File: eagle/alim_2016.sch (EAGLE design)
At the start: 54 parts, among them J1 AVR_SPI_PRG_6PTH, J2 AVR_SPI_PRG_6PTH, U1 3.3V, U2 LM2678S-5.0, U4 LM2596S-ADJ, U5 ATTINY85-20SU, U6 ATMEGA328P_TQFP

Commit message: clean up board
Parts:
- added C5: 10n, rcl:C-EUC0805
- added U$29: SRR1260, alim:SRR1260
- added U$30: SBRS8340, alim:SBRS8340
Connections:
- net N$12 renamed 24V
- new net N$29: C5.2, U$29.1, U$30.P$2, U2.SW
- new net N$30: C5.1, U2.BOOST
- net 5.0V: now also U$29.2, U2.FB
- net GND: now also U$30.P$1
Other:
- moved on the sheet: U2
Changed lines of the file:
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@@
 <layer number="230" name="230bmp" color="7" fill="1" visible="yes" active="yes"/>
 <layer number="231" name="231bmp" color="7" fill="1" visible="yes" active="yes"/>
+<layer number="232" name="Eagle3D_PG2" color="7" fill="1" visible="no" active="no"/>
+<layer number="233" name="Eagle3D_PG3" color="7" fill="1" visible="no" active="no"/>
 <layer number="248" name="Housing" color="7" fill="1" visible="yes" active="yes"/>
 <layer number="249" name="Edge" color="7" fill="1" visible="yes" active="yes"/>
@@
 <part name="R19" library="resistor" deviceset="R-EU_" device="M0805" value="220"/>
 <part name="U$28" library="microbuilder" deviceset="GND" device=""/>
+<part name="U$29" library="alim" deviceset="SRR1260" device=""/>
+<part name="C5" library="rcl" deviceset="C-EU" device="C0805" value="10n"/>
+<part name="U$30" library="alim" deviceset="SBRS8340" device=""/>
+<part name="U$31" library="microbuilder" deviceset="GND" device=""/>
+<part name="U$32" library="microbuilder" deviceset="5.0V" device=""/>
 </parts>
 <sheets>
@@
 <instance part="U$7" gate="G$1" x="124.46" y="-12.7"/>
 <instance part="U2" gate="A" x="106.68" y="55.88"/>
-<instance part="U$22" gate="G$1" x="88.9" y="45.72"/>
+<instance part="U$22" gate="G$1" x="106.68" y="43.18"/>
 <instance part="U4" gate="A" x="104.14" y="22.86"/>
 <instance part="U$23" gate="G$1" x="88.9" y="10.16"/>
@@
 <instance part="R5" gate="G$1" x="-27.94" y="30.48" rot="R180"/>
 <instance part="S1" gate="G$1" x="-22.86" y="38.1" rot="MR90"/>
-<instance part="U$4" gate="G$1" x="88.9" y="58.42"/>
+<instance part="U$4" gate="G$1" x="88.9" y="55.88"/>
 <instance part="12V" gate="-1" x="-2.54" y="43.18"/>
 <instance part="12V" gate="-2" x="-2.54" y="22.86"/>
@@
 <instance part="R19" gate="G$1" x="142.24" y="-91.44" rot="R180"/>
 <instance part="U$28" gate="G$1" x="147.32" y="-99.06"/>
+<instance part="U$29" gate="G$1" x="124.46" y="50.8"/>
+<instance part="C5" gate="G$1" x="114.3" y="55.88" rot="R90"/>
+<instance part="U$30" gate="G$1" x="119.38" y="45.72" rot="R270"/>
+<instance part="U$31" gate="G$1" x="119.38" y="40.64"/>
+<instance part="U$32" gate="G$1" x="134.62" y="53.34"/>
 </instances>
 <busses>
@@
 <pinref part="U$22" gate="G$1" pin="GND"/>
 <pinref part="U2" gate="A" pin="GND_2"/>
-<wire x1="88.9" y1="50.8" x2="88.9" y2="48.26" width="0.1524" layer="91"/>
-<junction x="88.9" y="48.26"/>
+<junction x="106.68" y="45.72"/>
+<wire x1="106.68" y1="45.72" x2="104.14" y2="45.72" width="0.1524" layer="91"/>
 </segment>
 <segment>
@@
 <pinref part="U$28" gate="G$1" pin="GND"/>
 </segment>
+<segment>
+<pinref part="U$30" gate="G$1" pin="P$1"/>
+<pinref part="U$31" gate="G$1" pin="GND"/>
+</segment>
 </net>
 <net name="5.0V" class="0">
@@
 <pinref part="5V" gate="-1" pin="K"/>
 <pinref part="U$3" gate="G$1" pin="5.0V"/>
+</segment>
+<segment>
+<pinref part="U2" gate="A" pin="FB"/>
+<wire x1="101.6" y1="60.96" x2="129.54" y2="60.96" width="0.1524" layer="91"/>
+<pinref part="U$29" gate="G$1" pin="2"/>
+<wire x1="129.54" y1="60.96" x2="129.54" y2="50.8" width="0.1524" layer="91"/>
+<pinref part="U$32" gate="G$1" pin="5.0V"/>
+<wire x1="129.54" y1="50.8" x2="134.62" y2="50.8" width="0.1524" layer="91"/>
+<junction x="129.54" y="50.8"/>
 </segment>
 </net>
@@
 </segment>
 </net>
-<net name="N$12" class="0">
+<net name="24V" class="0">
 <segment>
 <pinref part="BAT2" gate="-1" pin="KL"/>
@@
 <pinref part="U2" gate="A" pin="VIN"/>
 <pinref part="U$4" gate="G$1" pin="12V"/>
+<wire x1="88.9" y1="53.34" x2="91.44" y2="53.34" width="0.1524" layer="91"/>
 </segment>
 </net>
@@
 </segment>
 </net>
+<net name="N$29" class="0">
+<segment>
+<pinref part="U2" gate="A" pin="SW"/>
+<pinref part="U$29" gate="G$1" pin="1"/>
+<pinref part="C5" gate="G$1" pin="2"/>
+<wire x1="119.38" y1="55.88" x2="119.38" y2="50.8" width="0.1524" layer="91"/>
+<junction x="119.38" y="50.8"/>
+<wire x1="119.38" y1="50.8" x2="111.76" y2="50.8" width="0.1524" layer="91"/>
+<pinref part="U$30" gate="G$1" pin="P$2"/>
+</segment>
+</net>
+<net name="N$30" class="0">
+<segment>
+<pinref part="U2" gate="A" pin="BOOST"/>
+<pinref part="C5" gate="G$1" pin="1"/>
+</segment>
+</net>

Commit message: most of the circuit finished
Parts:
- 12V, 24V, 3.3V, 5V, 8V: value 1751248 -> MKDSN1,5/2-5,08; device con-phoenix-350:1751248 -> con-phoenix-508:MKDSN1,5/2-5,08
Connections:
- net 12V: now also 12V-1.KL; no longer 12V-1.K
- net 24V: now also 24V-1.KL; no longer 24V-1.K
- net 5.0V: now also 5V-1.KL; no longer 5V-1.K
- net GND: now also 12V-2.KL, 24V-2.KL, 3.3V-2.KL, 5V-2.KL, 8V-2.KL; no longer 12V-2.K, 24V-2.K, 3.3V-2.K, 5V-2.K, 8V-2.K
- net N$1: now also 3.3V-1.KL; no longer 3.3V-1.K
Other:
- moved on the sheet: BAT1-1, BAT1-2, BAT2-1, BAT2-2, BAT3-1, BAT3-2, C1, C2, C3, C4, C5, D1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

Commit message: more cleanup
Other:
- moved on the sheet: D1, D2, D3, D4, LED1, LED2, LED3, LED4, LED5, LED6, R10, R11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

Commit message: rearrange stuff
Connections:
- net N$29 renamed SW
- net N$30 renamed BOOST
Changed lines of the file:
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@@
 </segment>
 </net>
-<net name="N$29" class="0">
+<net name="SW" class="0">
 <segment>
 <pinref part="U2" gate="A" pin="SW"/>
@@
 </segment>
 </net>
-<net name="N$30" class="0">
+<net name="BOOST" class="0">
 <segment>
 <pinref part="U2" gate="A" pin="BOOST"/>

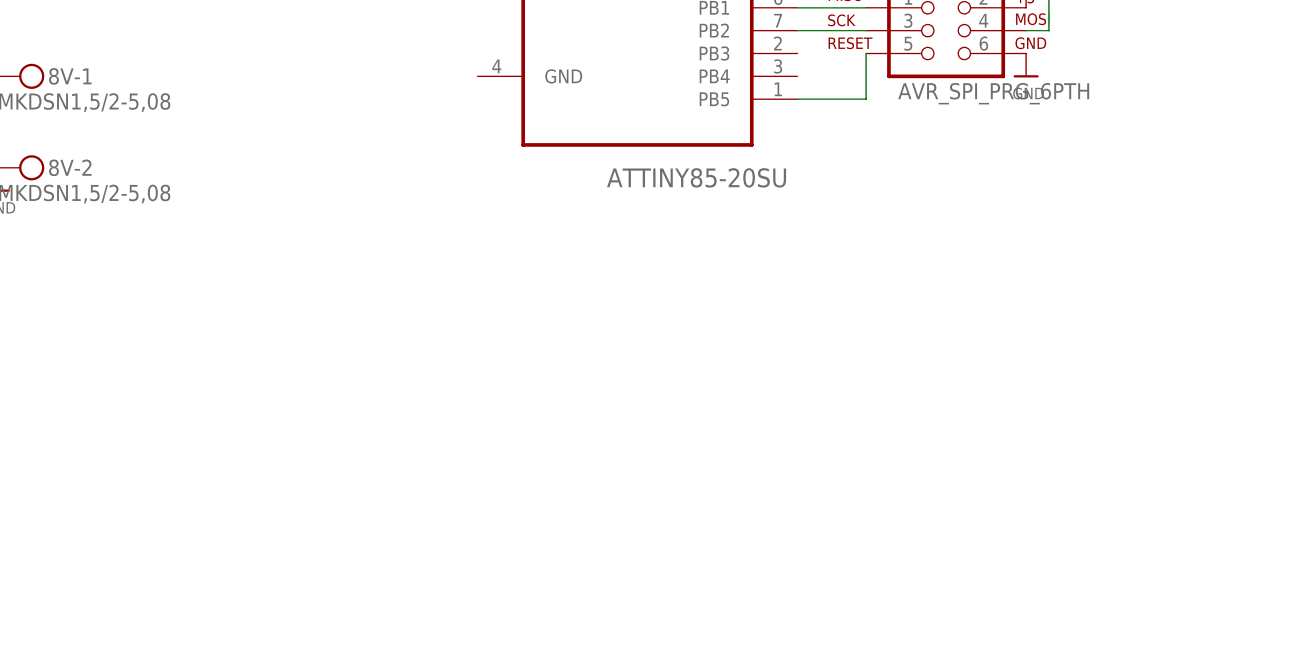
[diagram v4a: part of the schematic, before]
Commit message: add new switching regulator
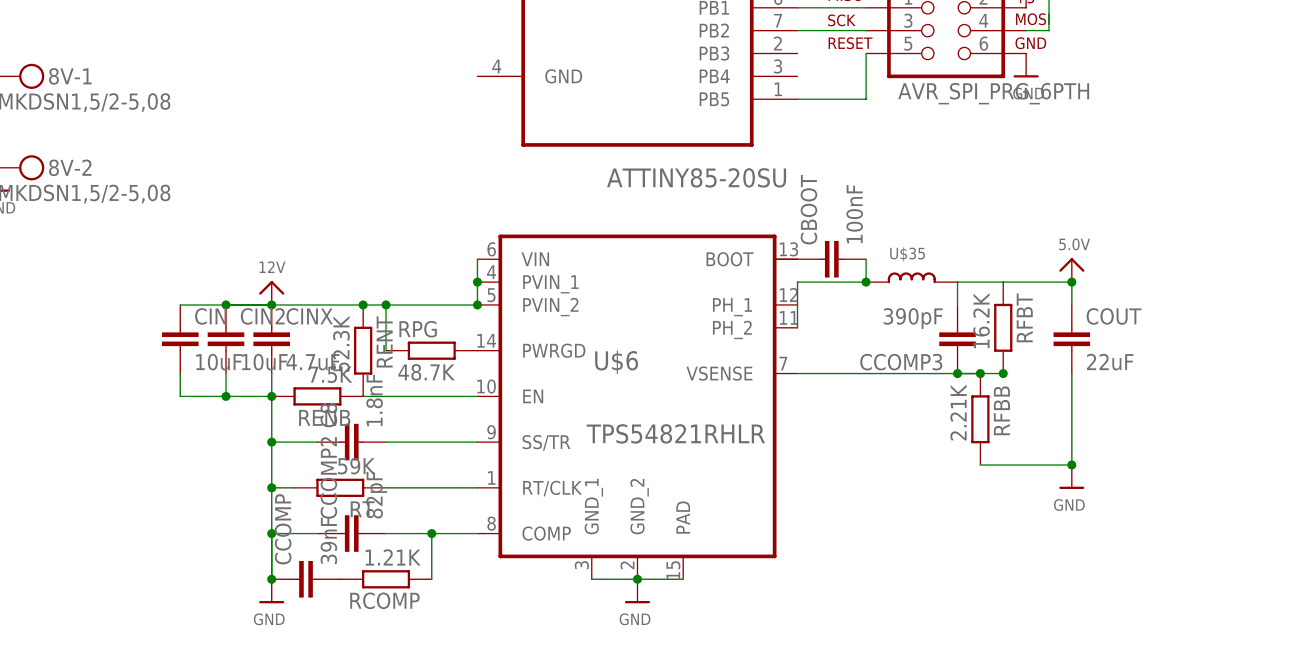
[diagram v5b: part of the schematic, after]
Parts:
- added C8: 1.8nF, rcl:C-EUC0805
- added CBOOT: 100nF, rcl:C-EUC0805
- added CCOMP: 39nF, rcl:C-EUC0805
- added CCOMP2: 82pF, rcl:C-EUC0805
- added CCOMP3: 390pF, rcl:C-EUC0805
- added CIN, CIN2: 10uF, rcl:C-EUC0805
- added CINX: 4.7uF, rcl:C-EUC0805
- added COUT: 22uF, rcl:C-EUC0805
- added RCOMP: 1.21K, resistor:R-EU_M0805
- added RENB: 7.5K, resistor:R-EU_M0805
- added RENT: 52.3K, resistor:R-EU_M0805
- added RFBB: 2.21K, resistor:R-EU_M0805
- added RFBT: 16.2K, resistor:R-EU_M0805
- added RPG: 48.7K, resistor:R-EU_M0805
- added RT: 59K, resistor:R-EU_M0805
- added U$35: 2.2uH, alim:XAL5030
- added U$6: TPS54821RHLR, alim:TPS54821RHLR
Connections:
- new net COMP: CCOMP2.2, RCOMP.1, U$6.COMP
- new net EN: RENB.1, RENT.2, U$6.EN
- new net N$30: CCOMP.2, RCOMP.2
- new net N$31: CBOOT.1, U$6.BOOT
- new net N$35: RPG.2, U$6.PWRGD
- new net PH: CBOOT.2, U$35.1, U$6.PH_1, U$6.PH_2
- new net RTCLK: RT.1, U$6.RT/CLK
- new net SSTR: C8.2, U$6.SS/TR
- new net VSENSE: CCOMP3.1, RFBB.1, RFBT.2, U$6.VSENSE
- net 12V: now also CIN.1, CIN2.1, CINX.1, RENT.1, RPG.1, U$6.PVIN_1, U$6.PVIN_2, U$6.VIN
- net 5.0V: now also CCOMP3.2, COUT.1, RFBT.1, U$35.2
- net GND: now also C8.1, CCOMP.1, CCOMP2.1, CIN.2, CIN2.2, CINX.2, COUT.2, RENB.2, RFBB.2, RT.2, U$6.GND_1, U$6.GND_2, U$6.PAD

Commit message: route TPS chip
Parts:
- removed C3, C4: (no value), rcl:C-EUC0805
- removed Q1: (no value), crystal:CRYSTALHC49S
- removed U$19, U$20: CSD19536KTT, alim:CSD19536KTT
- added C12: 0.1uF, rcl:C-EUC0805
- added U$38, U$39: IRFR8314TRPBF, alim:IRFR8314TRPBF
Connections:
- removed net N$6: C3.2, Q1.2, U6.PB6(XTAL1/TOSC1)
- removed net N$7: C4.2, Q1.1, U6.PB7(XTAL2/TOSC2)
- net 5.0V: now also C12.1
- net BAT12_CUT: now also U$38.G; no longer U$19.G
- net BAT24_CUT: now also U$39.G; no longer U$20.G
- net GND: now also C12.2, U$38.D, U$39.D; no longer C3.1, C4.1, U$19.D, U$20.D
- net N$13: now also U$38.S; no longer U$19.S
- net N$8: now also U$39.S; no longer U$20.S
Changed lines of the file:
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@@
 <part name="R1" library="resistor" deviceset="R-EU_" device="M0805" value="10K"/>
 <part name="U$15" library="microbuilder" deviceset="5.0V" device=""/>
-<part name="Q1" library="crystal" deviceset="CRYSTAL" device="HC49S"/>
-<part name="C3" library="rcl" deviceset="C-EU" device="C0805"/>
-<part name="C4" library="rcl" deviceset="C-EU" device="C0805"/>
-<part name="U$16" library="microbuilder" deviceset="GND" device=""/>
 <part name="24V" library="con-phoenix-508" deviceset="MKDSN1,5/2-5,08" device=""/>
 <part name="5V" library="con-phoenix-508" deviceset="MKDSN1,5/2-5,08" device=""/>
@@
 <part name="U4" library="alim" deviceset="LM2596S-ADJ" device=""/>
 <part name="U$23" library="microbuilder" deviceset="GND" device=""/>
-<part name="U$19" library="alim" deviceset="CSD19536KTT" device=""/>
-<part name="U$20" library="alim" deviceset="CSD19536KTT" device=""/>
 <part name="U5" library="alim" deviceset="ATTINY85-20SU" device=""/>
 <part name="J2" library="SparkFun-Connectors" deviceset="AVR_SPI_PRG_6" device="PTH"/>
@@
 <part name="CIN2" library="rcl" deviceset="C-EU" device="C0805" value="10uF"/>
 <part name="CIN" library="rcl" deviceset="C-EU" device="C0805" value="10uF"/>
+<part name="U$38" library="alim" deviceset="IRFR8314TRPBF" device=""/>
+<part name="U$39" library="alim" deviceset="IRFR8314TRPBF" device=""/>
+<part name="C12" library="rcl" deviceset="C-EU" device="C0805" value="0.1uF"/>
+<part name="U$16" library="microbuilder" deviceset="GND" device=""/>
 </parts>
 <sheets>
@@
 <instance part="R1" gate="G$1" x="73.66" y="55.88" rot="MR90"/>
 <instance part="U$15" gate="G$1" x="73.66" y="63.5" rot="MR0"/>
-<instance part="Q1" gate="G$1" x="71.12" y="22.86" rot="MR90"/>
-<instance part="C3" gate="G$1" x="76.2" y="25.4" rot="MR90"/>
-<instance part="C4" gate="G$1" x="76.2" y="20.32" rot="MR90"/>
-<instance part="U$16" gate="G$1" x="81.28" y="17.78" rot="MR0"/>
 <instance part="24V" gate="-1" x="-71.12" y="15.24"/>
 <instance part="24V" gate="-2" x="-71.12" y="-5.08"/>
@@
 <instance part="U4" gate="A" x="-106.68" y="-58.42"/>
 <instance part="U$23" gate="G$1" x="-121.92" y="-71.12"/>
-<instance part="U$19" gate="A" x="-99.06" y="27.94" rot="R270"/>
-<instance part="U$20" gate="A" x="-81.28" y="-2.54" rot="R270"/>
 <instance part="U5" gate="A" x="10.16" y="-48.26"/>
 <instance part="J2" gate="G$1" x="43.18" y="-50.8"/>
@@
 <instance part="CIN2" gate="G$1" x="-35.56" y="-83.82"/>
 <instance part="CIN" gate="G$1" x="-40.64" y="-83.82"/>
+<instance part="U$38" gate="G$1" x="-99.06" y="27.94" rot="R270"/>
+<instance part="U$39" gate="G$1" x="-81.28" y="-2.54" rot="R270"/>
+<instance part="C12" gate="G$1" x="73.66" y="40.64"/>
+<instance part="U$16" gate="G$1" x="73.66" y="33.02" rot="MR0"/>
 </instances>
 <busses>
@@
 <pinref part="U$8" gate="G$1" pin="GND"/>
 <pinref part="24V" gate="-2" pin="KL"/>
-<pinref part="U$20" gate="A" pin="D"/>
-<pinref part="U$20" gate="A" pin="D"/>
 <junction x="-73.66" y="-5.08"/>
 <junction x="-73.66" y="-5.08"/>
 <pinref part="LED8" gate="G$1" pin="C"/>
-<junction x="-76.2" y="-5.08"/>
 <wire x1="-73.66" y1="-5.08" x2="-76.2" y2="-5.08" width="0.1524" layer="91"/>
+<pinref part="U$39" gate="G$1" pin="D"/>
 </segment>
 <segment>
@@
 </segment>
 <segment>
-<pinref part="C3" gate="G$1" pin="1"/>
-<pinref part="C4" gate="G$1" pin="1"/>
-<wire x1="78.74" y1="25.4" x2="78.74" y2="22.86" width="0.1524" layer="91"/>
-<wire x1="78.74" y1="22.86" x2="78.74" y2="20.32" width="0.1524" layer="91"/>
-<wire x1="78.74" y1="22.86" x2="81.28" y2="22.86" width="0.1524" layer="91"/>
-<wire x1="81.28" y1="22.86" x2="81.28" y2="20.32" width="0.1524" layer="91"/>
-<junction x="78.74" y="22.86"/>
-<pinref part="U$16" gate="G$1" pin="GND"/>
-</segment>
-<segment>
 <pinref part="3.3V" gate="-2" pin="KL"/>
 <pinref part="U$7" gate="G$1" pin="GND"/>
@@
 <pinref part="U$17" gate="G$1" pin="GND"/>
 <pinref part="LED7" gate="G$1" pin="C"/>
-<pinref part="U$19" gate="A" pin="D"/>
 <wire x1="-93.98" y1="25.4" x2="-91.44" y2="25.4" width="0.1524" layer="91"/>
 <pinref part="12V" gate="-2" pin="KL"/>
@@
 <junction x="-83.82" y="25.4"/>
 <junction x="-91.44" y="25.4"/>
+<pinref part="U$38" gate="G$1" pin="D"/>
 </segment>
 <segment>
@@
 <junction x="58.42" y="-99.06"/>
 </segment>
+<segment>
+<pinref part="C12" gate="G$1" pin="2"/>
+<pinref part="U$16" gate="G$1" pin="GND"/>
+</segment>
 </net>
 <net name="5.0V" class="0">
@@
 <junction x="71.12" y="43.18"/>
 <pinref part="U6" gate="U$1" pin="VCC@6"/>
+<pinref part="C12" gate="G$1" pin="1"/>
+<junction x="73.66" y="43.18"/>
 </segment>
 <segment>
@@
 </segment>
 </net>
-<net name="N$6" class="0">
-<segment>
-<pinref part="Q1" gate="G$1" pin="2"/>
-<pinref part="C3" gate="G$1" pin="2"/>
-<junction x="71.12" y="25.4"/>
-<pinref part="C3" gate="G$1" pin="2"/>
-<pinref part="U6" gate="U$1" pin="PB6(XTAL1/TOSC1)"/>
-</segment>
-</net>
-<net name="N$7" class="0">
-<segment>
-<pinref part="Q1" gate="G$1" pin="1"/>
-<pinref part="C4" gate="G$1" pin="2"/>
-<junction x="71.12" y="20.32"/>
-<pinref part="C4" gate="G$1" pin="2"/>
-<pinref part="U6" gate="U$1" pin="PB7(XTAL2/TOSC2)"/>
-</segment>
-</net>
 <net name="RESET" class="0">
 <segment>
@@
 <segment>
 <pinref part="BAT1" gate="-2" pin="KL"/>
-<pinref part="U$20" gate="A" pin="S"/>
 <wire x1="-86.36" y1="-5.08" x2="-93.98" y2="-5.08" width="0.1524" layer="91"/>
 <pinref part="R2" gate="G$1" pin="2"/>
@@
 <pinref part="R18" gate="G$1" pin="1"/>
 <junction x="-104.14" y="-5.08"/>
+<pinref part="U$39" gate="G$1" pin="S"/>
 </segment>
 </net>
 <net name="BAT24_CUT" class="0">
 <segment>
-<pinref part="U$20" gate="A" pin="G"/>
 <pinref part="R2" gate="G$1" pin="1"/>
-<junction x="-83.82" y="0"/>
 <wire x1="-83.82" y1="0" x2="-83.82" y2="2.54" width="0.1524" layer="91"/>
 <wire x1="-83.82" y1="5.08" x2="-83.82" y2="2.54" width="0.1524" layer="91"/>
@@
 <pinref part="R3" gate="G$1" pin="2"/>
 <wire x1="-83.82" y1="5.08" x2="-76.2" y2="5.08" width="0.1524" layer="91"/>
+<pinref part="U$39" gate="G$1" pin="G"/>
+<junction x="-83.82" y="0"/>
 </segment>
 <segment>
@@
 <net name="N$13" class="0">
 <segment>
-<pinref part="U$19" gate="A" pin="S"/>
 <wire x1="-104.14" y1="25.4" x2="-111.76" y2="25.4" width="0.1524" layer="91"/>
 <pinref part="BAT3" gate="-2" pin="KL"/>
@@
 <wire x1="-111.76" y1="33.02" x2="-111.76" y2="25.4" width="0.1524" layer="91"/>
 <junction x="-111.76" y="25.4"/>
+<pinref part="U$38" gate="G$1" pin="S"/>
 </segment>
 </net>
 <net name="BAT12_CUT" class="0">
 <segment>
-<pinref part="U$19" gate="A" pin="G"/>
 <pinref part="R5" gate="G$1" pin="1"/>
 <pinref part="S1" gate="G$1" pin="1"/>
@@
 <wire x1="-101.6" y1="35.56" x2="-96.52" y2="35.56" width="0.1524" layer="91"/>
 <junction x="-101.6" y="35.56"/>
-</segment>
-<segment>
+<pinref part="U$38" gate="G$1" pin="G"/>
+</segment>
+<segment>

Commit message: cleanup
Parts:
- removed 8V: MKDSN1,5/2-5,08, con-phoenix-508:MKDSN1,5/2-5,08
- removed C5: 10n, rcl:C-EUC0805
- removed J2: AVR_SPI_PRG_6PTH, SparkFun-Connectors:AVR_SPI_PRG_6PTH
- removed U$29: SRR1260, alim:SRR1260
- removed U$30: SBRS8340, alim:SBRS8340
- removed U2: LM2678S-5.0, alim:LM2678S-5.0
- removed U5: ATTINY85-20SU, alim:ATTINY85-20SU
- added 5V1, 5V2, 5V3, 5V4: MKDSN1,5/2-5,08, con-phoenix-508:MKDSN1,5/2-5,08
- added SG1: F/CM12P, buzzer:F/CM12P
- LED2, LED5: value YELLOW -> YLW
- LED3, LED6: value GREEN -> GRN
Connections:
- removed net BOOST: C5.1, U2.BOOST
- removed net N$39: J2.1, U5.PB1
- removed net N$40: J2.4, U5.PB0
- removed net N$41: J2.3, U5.PB2
- removed net N$42: J2.5, U5.PB5
- removed net SW: C5.2, U$29.1, U$30.P$2, U2.SW
- net 12V: no longer U2.VIN
- net 5.0V: now also 5V1-1.KL, 5V2-1.KL, 5V3-1.KL, 5V4-1.KL; no longer J2.2, U$29.2, U2.FB
- net GND: now also 5V1-2.KL, 5V2-2.KL, 5V3-2.KL, 5V4-2.KL; no longer 8V-2.KL, J2.6, U$30.P$1, U2.GND, U2.GND_2
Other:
- moved on the sheet: D2, D3, D4

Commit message: changed connectors
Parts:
- removed 5V, 5V1, 5V2, 5V3, 5V4: MKDSN1,5/2-5,08, con-phoenix-508:MKDSN1,5/2-5,08
- added 5V_1, 5V_2, 5V_3, 5V_4, 5V_5: WURTH_2PIN311, alim:WURTH_2PIN311
- added MTRSTP: M02PTH, SparkFun-Connectors:M02PTH
- added R20, R21: 10K, resistor:R-EU_M0805
- 12V, 24V, 3.3V: value MKDSN1,5/2-5,08 -> WURTH_2PIN311; device con-phoenix-508:MKDSN1,5/2-5,08 -> alim:WURTH_2PIN311
- BAT1, BAT2, BAT3: value (none) -> WURTH_2PIN313; device con-ptr500:AK300/2 -> alim:WURTH_2PIN313
- S1: value SWITCH-MOMENTARY-2PTH -> MOMENTARY-SWITCH3LEG; device SparkFun-Electromechanical:SWITCH-MOMENTARY-2PTH -> alim:MOMENTARY-SWITCH3LEG
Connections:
- new net N$6: MTRSTP.1, R20.2, U6.PD5(T1)
- new net N$7: R21.2, S1.2
- net 12V: now also R21.1; no longer S1.2
- net 5.0V: now also 5V_1-1.KL, 5V_2-1.KL, 5V_3-1.KL, 5V_4-1.KL, 5V_5-1.KL, R20.1; no longer 5V-1.KL, 5V1-1.KL, 5V2-1.KL, 5V3-1.KL, 5V4-1.KL
- net GND: now also 5V_1-2.KL, 5V_2-2.KL, 5V_3-2.KL, 5V_4-2.KL, 5V_5-2.KL, MTRSTP.2; no longer 5V-2.KL, 5V1-2.KL, 5V2-2.KL, 5V3-2.KL, 5V4-2.KL
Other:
- moved on the sheet: 12V-1, BAT1-1, BAT1-2, BAT2-1, BAT2-2, BAT3-1, BAT3-2, D1, LED1, LED2, LED3, R11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
